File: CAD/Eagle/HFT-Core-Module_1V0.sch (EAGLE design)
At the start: 399 parts, among them Q0521 ABS07-32.768KHZ, Q0811 ABM03B-32.000MHZ, Q0911 ABM3B-16MHZ-10-R50-1-U, T1201 MMBT2222, T1202 MMBT2222, T1203 MMBT2222, U0111 STM32L4Z_144PIN_SMPS, U0431 PAM2305AAB120, U0601 LM4120IM5-3.0, U0611 MAX5217, U0631 CFPT-141-20MHZ, U0641 OPA354, U0701 Si5338, U0801 SX1276, U0901 AX5243, U0911 PE4259, U0921 PE4259, U0991 PE4259, U1101 MCP3911A0-E-SS, U1111 MAX5136AGTG+, U1121 OPA354, U1131 OPA354, U1141 OPA354, U1201 NHD-C0220BIZ_2X20CHARS, U1301 MPU-9250, U1311 MS5607-02BA03, U1321 SHT31-DIS, U1401 SOLARPANEL_3V3_5MA1_25MM_X_20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, U1402 SPV1040T, U1501 TS5A23166, U1601 SC189ZSKTRT, U1701 TS5A23166, U1801 TS5A23166, U1901 TS5A23166, X1261 TTE_EN11-HSM, X2001 MOLEX 105017-0001, X2101 SMA_SMT_AMPHENOL-901-143, SAM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, X2111 SMA_SMT_AMPHENOL-901-143, SAM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, X2201 CUI SJ1-3535NS, X2211 CUI SJ1-3535NS, X2311 2X20/90_1MM27_HARWIN_M50-3202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, X2312 2X20/90_1MM27_HARWIN_M50-3202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, X2321 2X20/90_1MM27_HARWIN_M50-3202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, X2322 2X20/90_1MM27_HARWIN_M50-3202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, X2331 2X20/90_1MM27_HARWIN_M50-3202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, X2332 2X20/90_1MM27_HARWIN_M50-3202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

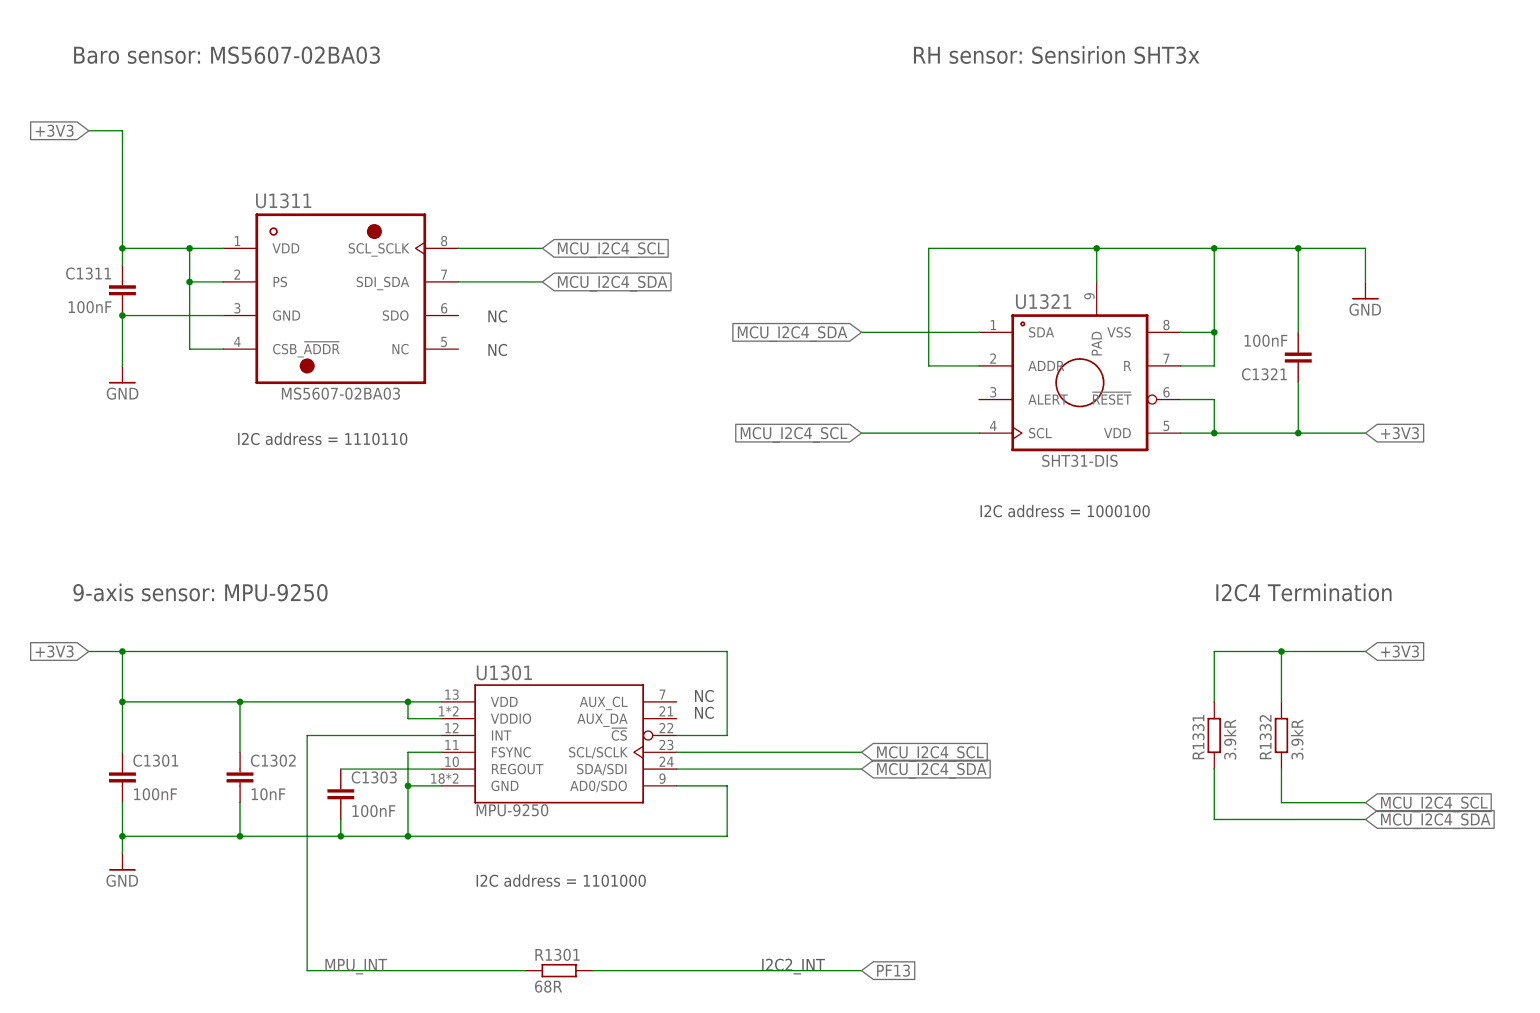
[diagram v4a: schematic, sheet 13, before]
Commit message: HW_1V0 - I2C R values and addresses changed
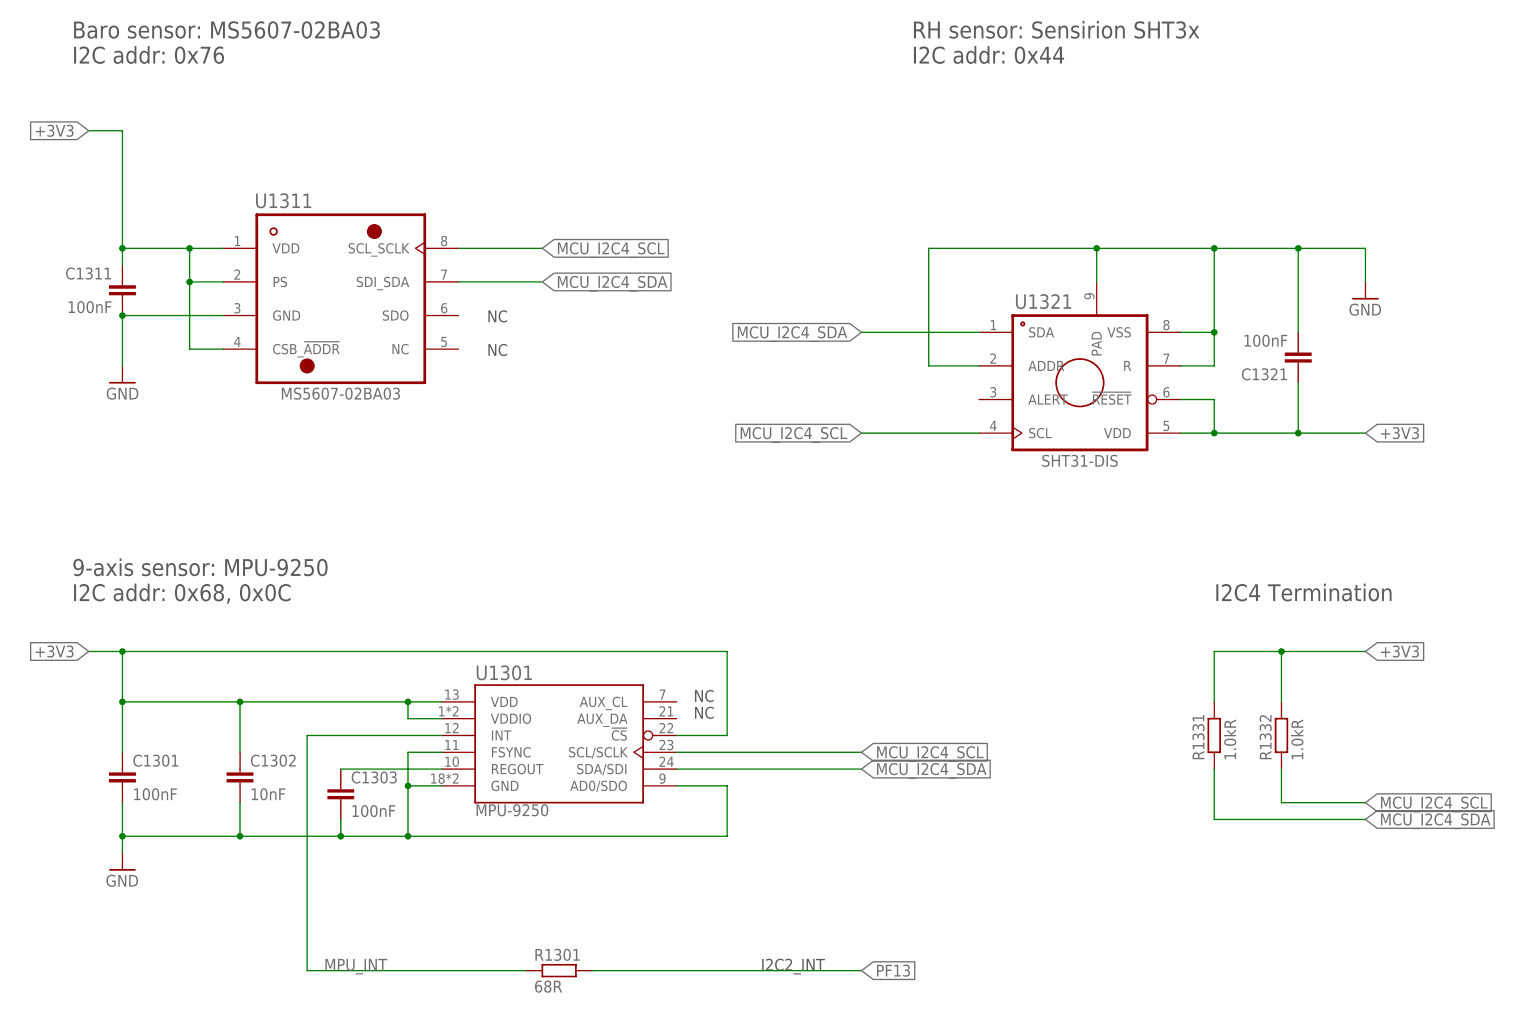
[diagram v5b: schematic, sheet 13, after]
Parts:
- R1331, R1332: value 3.9kR -> 1.0kR
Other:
- note added: "9-axis sensor: MPU-9250 I2C addr: 0x68, 0x0C"
- note added: "Baro sensor: MS5607-02BA03 I2C addr: 0x76"
- note added: "Clock distributor I2C addr: 0x70"
- note added: "D/A-Converter: I2C addr: 0x1C"
- note added: "LC-Display I2C addr: 0x3E"
- note added: "RH sensor: Sensirion SHT3x I2C addr: 0x44"
- note removed: "9-axis sensor: MPU-9250"
- note removed: "Baro sensor: MS5607-02BA03"
- note removed: "Clock distributor I2C addr: 0xE0/0xE1"
- note removed: "D/A-Converter: I2C addr: 0x38/0x39"
- note removed: "I2C address = 1000100"
- note removed: "I2C address = 1101000"
- note removed: "I2C address = 1110110"
- note removed: "LC-Display I2C addr: 0x7C/0x7D"
- note removed: "RH sensor: Sensirion SHT3x"
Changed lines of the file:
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@@
 <part name="R1301" library="rcl" deviceset="R-EU_" device="R0603" value="68R"/>
 <part name="C1302" library="rcl" deviceset="C-EU" device="C0603" value="10nF"/>
-<part name="R1331" library="rcl" deviceset="R-EU_" device="R0603" value="3.9kR"/>
-<part name="R1332" library="rcl" deviceset="R-EU_" device="R0603" value="3.9kR"/>
+<part name="R1331" library="rcl" deviceset="R-EU_" device="R0603" value="1.0kR"/>
+<part name="R1332" library="rcl" deviceset="R-EU_" device="R0603" value="1.0kR"/>
 <part name="GND1311" library="df4iah_supply" deviceset="GND" device=""/>
 <part name="C1311" library="rcl" deviceset="C-EU" device="C0603" value="100nF"/>
@@
 <text x="182.88" y="162.56" size="2.54" layer="97" ratio="15">VCTCXO</text>
 <text x="22.86" y="162.56" size="2.54" layer="97" ratio="15">D/A-Converter:
-I2C addr: 0x38/0x39</text>
+I2C addr: 0x1C</text>
 <text x="208.28" y="48.26" size="1.778" layer="97">ADC3_IN6_20MHZ_PULL</text>
 </plain>
@@
 <text x="116.84" y="137.16" size="1.778" layer="97" rot="R90">Impedance 100 Ohms</text>
 <text x="22.86" y="162.56" size="2.54" layer="97" ratio="15">Clock distributor
-I2C addr: 0xE0/0xE1</text>
+I2C addr: 0x70</text>
 <text x="118.364" y="38.1" size="1.778" layer="97" rot="R90">10MHz</text>
 <text x="50.8" y="88.9" size="1.778" layer="97">16MHz</text>
@@
 <text x="160.02" y="139.7" size="1.778" layer="97">LCD: 2x20 chars  NHD-C0220BIZ-FS(RGB)-FBW-3VM-ND</text>
 <text x="22.86" y="162.56" size="2.54" layer="97" ratio="15">LC-Display
-I2C addr: 0x7C/0x7D</text>
+I2C addr: 0x3E</text>
 <text x="10.16" y="71.12" size="2.54" layer="97" ratio="15">Rotary Encoder with Pushbutton</text>
 <text x="15.24" y="139.7" size="1.778" layer="97" rot="R90">MCU_PWM_LED_R</text>
@@
 <description>I2C Sensors</description>
 <plain>
-<text x="22.86" y="162.56" size="2.54" layer="97" ratio="15">Baro sensor: MS5607-02BA03</text>
-<text x="22.86" y="81.28" size="2.54" layer="97" ratio="15">9-axis sensor: MPU-9250</text>
+<text x="22.86" y="162.56" size="2.54" layer="97" ratio="15">Baro sensor: MS5607-02BA03
+I2C addr: 0x76</text>
+<text x="22.86" y="81.28" size="2.54" layer="97" ratio="15">9-axis sensor: MPU-9250
+I2C addr: 0x68, 0x0C</text>
 <text x="116.84" y="66.04" size="1.778" layer="97">NC</text>
 <text x="116.84" y="63.5" size="1.778" layer="97">NC</text>
-<text x="83.82" y="38.1" size="1.778" layer="97">I2C address = 1101000</text>
-<text x="47.752" y="104.902" size="1.778" layer="97">I2C address = 1110110</text>
 <text x="85.598" y="118.364" size="1.778" layer="97">NC</text>
 <text x="85.598" y="123.444" size="1.778" layer="97">NC</text>
-<text x="149.86" y="162.56" size="2.54" layer="97" ratio="15">RH sensor: Sensirion SHT3x</text>
-<text x="160.02" y="93.98" size="1.778" layer="97">I2C address = 1000100</text>
+<text x="149.86" y="162.56" size="2.54" layer="97" ratio="15">RH sensor: Sensirion SHT3x
+I2C addr: 0x44</text>
 <text x="195.58" y="81.28" size="2.54" layer="97" ratio="15">I2C4 Termination</text>
 <text x="127" y="25.4" size="1.778" layer="97">I2C2_INT</text>

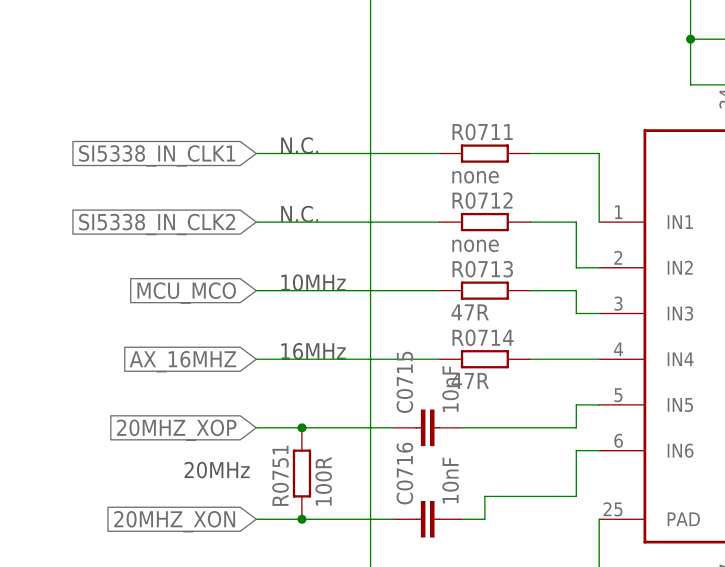
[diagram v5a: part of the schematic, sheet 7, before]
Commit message: HW_1V0 - Solar DC/DC needs 100uF at the input, MCU runs 24MHz and emits 12MHz for the Si5338
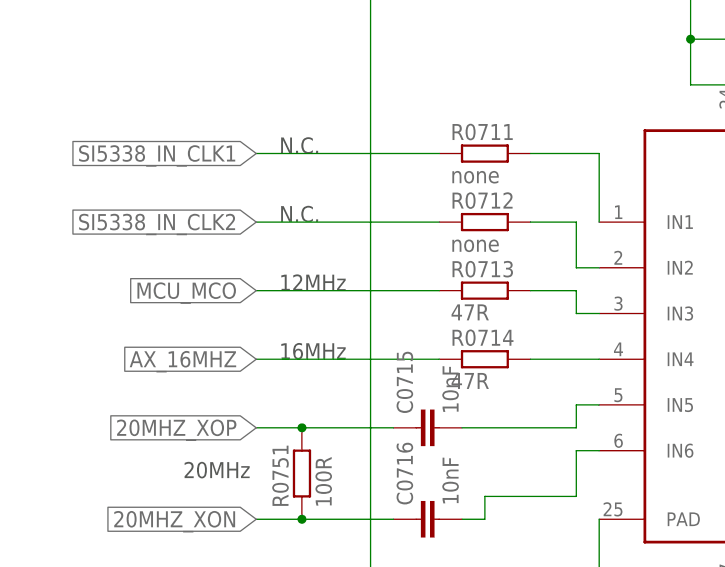
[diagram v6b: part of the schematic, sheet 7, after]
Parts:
- C1401: value 10uF -> 100uF
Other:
- note added: "12MHz"
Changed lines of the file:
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@@
 <part name="L1403" library="df4iah_rcl" deviceset="L-EU" device="13.5X12.5MM" value="33uH"/>
 <part name="C1403" library="rcl" deviceset="C-EU" device="C0603" value="100nF"/>
-<part name="C1401" library="rcl" deviceset="C-EU" device="C0805" value="10uF"/>
+<part name="C1401" library="rcl" deviceset="C-EU" device="C0805" value="100uF"/>
 <part name="C1402" library="rcl" deviceset="C-EU" device="C0603" value="100nF"/>
 <part name="C1404" library="rcl" deviceset="C-EU" device="C0805" value="10uF"/>
@@
 <text x="50.8" y="111.76" size="1.778" layer="97">N.C.</text>
 <text x="50.8" y="104.14" size="1.778" layer="97">N.C.</text>
-<text x="50.8" y="96.52" size="1.778" layer="97">10MHz</text>
+<text x="50.8" y="96.52" size="1.778" layer="97">12MHz</text>
 <text x="101.6" y="23.622" size="1.778" layer="97" rot="R90">MCU_EXTI7_INTR_SI5338</text>
 <text x="122.936" y="22.098" size="1.778" layer="97" rot="R90">MCU_HSE</text>

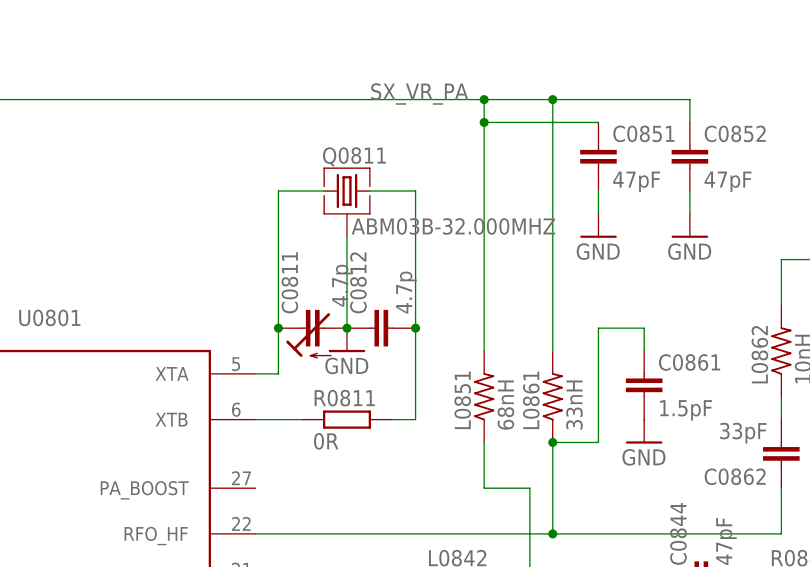
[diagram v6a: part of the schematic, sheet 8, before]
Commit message: HW_1V0 - SX1276 change of cap to 12pF
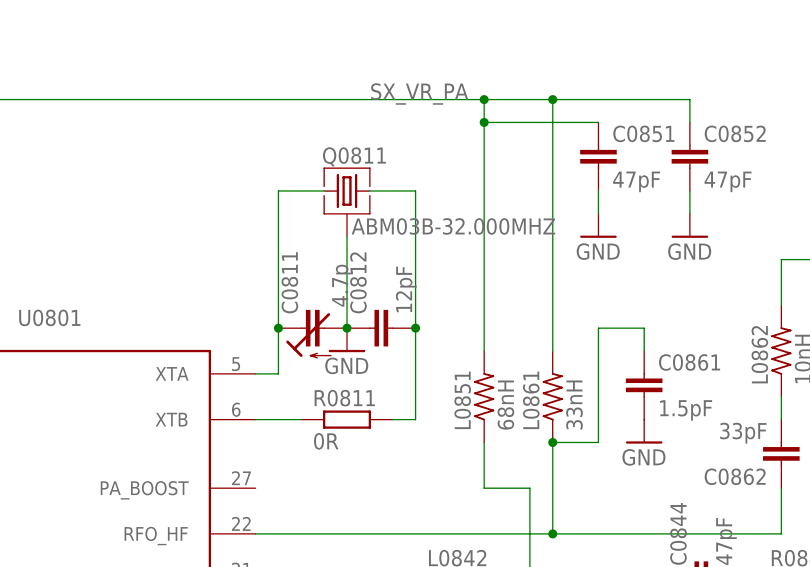
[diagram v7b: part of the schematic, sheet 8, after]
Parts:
- C0812: value 4.7p -> 12pF
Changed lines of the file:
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@@
 <part name="GND0811" library="df4iah_supply" deviceset="GND" device=""/>
 <part name="C0811" library="df4iah_c-trimm" deviceset="C-TRIMM" device="3MM2_2MM5" value="4.7p"/>
-<part name="C0812" library="rcl" deviceset="C-EU" device="C0603" value="4.7p"/>
+<part name="C0812" library="rcl" deviceset="C-EU" device="C0603" value="12pF"/>
 <part name="C0806" library="rcl" deviceset="C-EU" device="C0603" value="100n"/>
 <part name="C0807" library="rcl" deviceset="C-EU" device="C0603" value="100n"/>
